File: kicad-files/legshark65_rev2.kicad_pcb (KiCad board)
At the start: 2 copper layers, 285.8 x 97 mm, 202 parts, among them J1 ARM JTAG, J2 Conn_01x04, SW1 K2-1187SQ-A4SW-06, SW2 PCM12SMTR, T2 53261-0471, U1 STM32F411CEU6, U2 MCP1700T-3302E/TT, U3 AT24C256C-SSHL-T, Y1 TAXM8M4RFDCET2T

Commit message: Started adding all of the components onto the board
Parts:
- removed J2: Conn_01x04, acheron_Connectors:PinHeader_1x4_P2.54mm_Vertical
- removed R2, R3: 0R, Resistor_SMD:R_0603_1608Metric
- J1: moved to F.Cu
- moved J1 177.1 mm to (278.6, 17.8), turned to 90 degrees
- moved T2 129.6 mm to (142.9, 38.1), turned to 0 degrees
- moved R15 106.6 mm to (172.3, 34.5)
- moved C3 105.4 mm to (152.1, 39.0)
- moved R9 105.4 mm to (153.5, 36.2)
- moved U2 105.4 mm to (157.4, 35.5)
- moved C5 105.4 mm to (152.1, 41.5)
- moved D1 105.4 mm to (156.9, 39.4)
- moved R4 105.4 mm to (153.5, 34.2)
- moved C17 101.6 mm to (168.7, 34.8)
- moved C16 100.5 mm to (130.0, 36.9), turned to 0 degrees
- moved SW2 100.3 mm to (172.0, 39.6)
- moved SW1 69.9 mm to (152.4, 76.2)
- moved R11 67.6 mm to (153.6, 71.4)
- moved C7 62.4 mm to (150.0, 71.4)
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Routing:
- net Net-(D_15-A): track 0.00 -> 24.5 mm
- net Net-(D_61-A): track 0.00 -> 24.4 mm
- net Net-(D_45-A): track 0.00 -> 23.8 mm
- net Net-(D_66-A): track 0.00 -> 20.1 mm
- net Net-(D_60-A): track 0.00 -> 19.7 mm
- net Net-(D_68-A): track 0.00 -> 18.7 mm
- net Net-(D_64-A): track 0.00 -> 18.7 mm
- net Net-(D_44-A): track 0.00 -> 18.5 mm
- net Net-(D_67-A): track 0.00 -> 14.9 mm
- net Net-(D_65-A): track 0.00 -> 14.9 mm
- net Net-(D_37-A): track 0.00 -> 14.9 mm
- net Net-(D_43-A): track 0.00 -> 14.2 mm
- net Net-(D_69-A): track 0.00 -> 14.0 mm
- net Net-(D_63-A): track 0.00 -> 14.0 mm
- net Net-(D_58-A): track 0.00 -> 9.20 mm
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
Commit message: Started running some test routes
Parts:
- moved J1 273.6 mm to (7.50, 54.7)
- moved U2 28.8 mm to (128.6, 35.5)
- moved R4 26.6 mm to (127.4, 39.3)
- moved T2 26.2 mm to (116.7, 38.1), turned to 90 degrees
- moved R9 23.9 mm to (129.8, 39.3)
- moved C5 19.8 mm to (132.4, 39.3)
- moved D1 16.4 mm to (140.5, 39.3)
- moved C3 16.3 mm to (135.7, 39.3)
- moved C6 12.2 mm to (165.5, 73.0)
- moved C16 10.7 mm to (140.5, 34.5)
- moved R7 9.73 mm to (165.5, 75.3)
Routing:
- net row3: track 0.00 -> 281.0 mm
- net row1: track 0.00 -> 281.0 mm
- net row2: track 0.00 -> 266.7 mm
- net row0: track 0.00 -> 266.7 mm
- net row4: track 0.00 -> 242.9 mm
- net unconnected-(U1-PB10-Pad21): track 0.00 -> 146.3 mm
- net BOOT1: track 0.00 -> 144.6 mm
- net unconnected-(U1-PB1-Pad19): track 0.00 -> 125.0 mm
- net unconnected-(U1-PA15-Pad38): track 0.00 -> 118.1 mm
- net unconnected-(U1-PB0-Pad18): track 0.00 -> 105.5 mm
- net unconnected-(U1-PB3-Pad39): track 0.00 -> 98.8 mm
- net unconnected-(U1-PA7-Pad17): track 0.00 -> 83.7 mm
- net unconnected-(U1-PB4-Pad40): track 0.00 -> 79.5 mm
- net unconnected-(U1-PA6-Pad16): track 0.00 -> 66.9 mm
- net unconnected-(U1-PB5-Pad41): track 0.00 -> 60.3 mm
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
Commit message: Added more routing and planning
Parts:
- moved C16 61.2 mm to (201.7, 35.2), turned to 180 degrees
- moved T2 59.5 mm to (176.2, 37.9), turned to -90 degrees
- moved R4 39.5 mm to (166.9, 40.2)
- moved R9 39.5 mm to (169.3, 40.2)
- moved C3 34.6 mm to (170.3, 38.2)
- moved C5 31.5 mm to (163.9, 39.2)
- moved U2 31.1 mm to (159.6, 38.6)
- moved D1 25.8 mm to (166.1, 36.6), turned to 0 degrees
- moved R15 19.1 mm to (172.8, 15.4)
- moved SW2 19.1 mm to (172.5, 20.5)
- moved C17 19.1 mm to (169.2, 15.7)
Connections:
- C1 pad 1: Net-(U1-PD1/OSC_OUT) -> GND
- C1 pad 2: GND -> Net-(U1-PD1/OSC_OUT)
- J1 pad 1: SWDIO -> SWCLK
- J1 pad 10: GND -> NRST
- J1 pad 2: SWCLK -> SWDIO
- J1 pad 5: BOOT0 -> BOOT1
- J1 pad 6: BOOT1 -> BOOT0
- J1 pad 9: NRST -> GND
- T2 pad 2: D+ -> D-
- T2 pad 3: D- -> D+
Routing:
- net D-: track 0.00 -> 41.7 mm
- net D+: track 0.00 -> 41.7 mm
- net unconnected-(U1-PB15/SPI2_MOSI-Pad28): track 0.00 -> 40.2 mm, vias 0 -> 2
- net unconnected-(U1-PB14-Pad27): track 0.00 -> 20.7 mm
- net unconnected-(U1-PC15/OSC32_OUT-Pad4): track 8.69 -> 28.4 mm, vias 0 -> 2
- net GND: track 3.02 -> 19.1 mm, vias 7 -> 10
- net SWCLK: track 0.00 -> 12.0 mm
- net SWDIO: track 0.00 -> 10.2 mm
- net 3V3: track 2.93 -> 6.25 mm, vias 0 -> 4
- net unconnected-(U1-PB12-Pad25): track 0.00 -> 3.11 mm
- net unconnected-(U1-PC14/OSC32_IN-Pad3): track 6.55 -> 8.98 mm
- net BOOT1: track 144.6 -> 142.7 mm
- net row2: track 266.7 -> 267.8 mm, vias 0 -> 2
- net unconnected-(U1-PB1-Pad19): track 125.0 -> 126.0 mm

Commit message: Started connecting more stuff
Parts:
- C1, C10, C11, C12, C13, C14, C15, C17, C2, C6, C7, C9: footprint Capacitor_SMD:C_0603_1608Metric_Pad1.08x0.95mm_HandSolder -> Capacitor_SMD:C_0402_1005Metric_Pad0.74x0.62mm_HandSolder
- C3, C5: footprint Capacitor_SMD:C_0603_1608Metric -> Capacitor_SMD:C_0402_1005Metric_Pad0.74x0.62mm_HandSolder
- R1, R11, R15, R5, R6, R7, R8: footprint Resistor_SMD:R_0603_1608Metric -> Resistor_SMD:R_0402_1005Metric_Pad0.72x0.64mm_HandSolder
- R4, R9: footprint Resistor_SMD:R_0402_1005Metric -> Resistor_SMD:R_0402_1005Metric_Pad0.72x0.64mm_HandSolder
- moved R6 117.0 mm to (21.8, 57.5)
- moved R5 101.5 mm to (158.9, 34.7), turned to -90 degrees
- moved R1 85.4 mm to (152.2, 46.6), turned to -90 degrees
- moved C10 80.9 mm to (157.7, 50.1), turned to -90 degrees
- moved C11 78.5 mm to (145.2, 52.7), turned to 0 degrees
- moved C15 77.3 mm to (145.1, 54.5), turned to 90 degrees
- moved C14 72.2 mm to (159.6, 61.3), turned to 0 degrees
- moved C9 69.2 mm to (159.6, 60.3)
- moved C12 65.6 mm to (148.2, 68.7)
- moved C13 58.6 mm to (145.8, 68.7), turned to 0 degrees
- moved R15 57.4 mm to (171.0, 72.8)
- moved C17 57.0 mm to (168.1, 72.7)
- moved SW2 55.7 mm to (171.4, 76.2)
- moved R8 22.0 mm to (199.4, 72.6)
- moved C6 20.3 mm to (185.7, 71.5)
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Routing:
- net 3V3: track 6.25 -> 64.4 mm, vias 4 -> 7
- net Net-(U1-PB6--I2C1_SCL): track 0.00 -> 26.9 mm, vias 0 -> 2
- net Net-(U1-PB7--I2C1_SDA): track 0.00 -> 25.8 mm, vias 0 -> 2
- net BOOT0: track 0.00 -> 24.9 mm, vias 0 -> 2
- net row2: track 267.8 -> 247.7 mm
- net GND: track 19.1 -> 30.5 mm
- net NRST: track 0.00 -> 10.2 mm
- net unconnected-(U1-PA1-Pad11): track 0.00 -> 9.26 mm
- net unconnected-(U1-PA0-WKUP-Pad10): track 0.00 -> 8.75 mm
- net unconnected-(U1-PA2-Pad12): track 0.00 -> 7.37 mm
- net Net-(U1-VCAP_1): track 0.00 -> 3.44 mm
- net Net-(U1-PD1/OSC_OUT): track 3.93 -> 5.41 mm
- net Net-(U1-PD0/OSC_IN): track 5.81 -> 7.29 mm

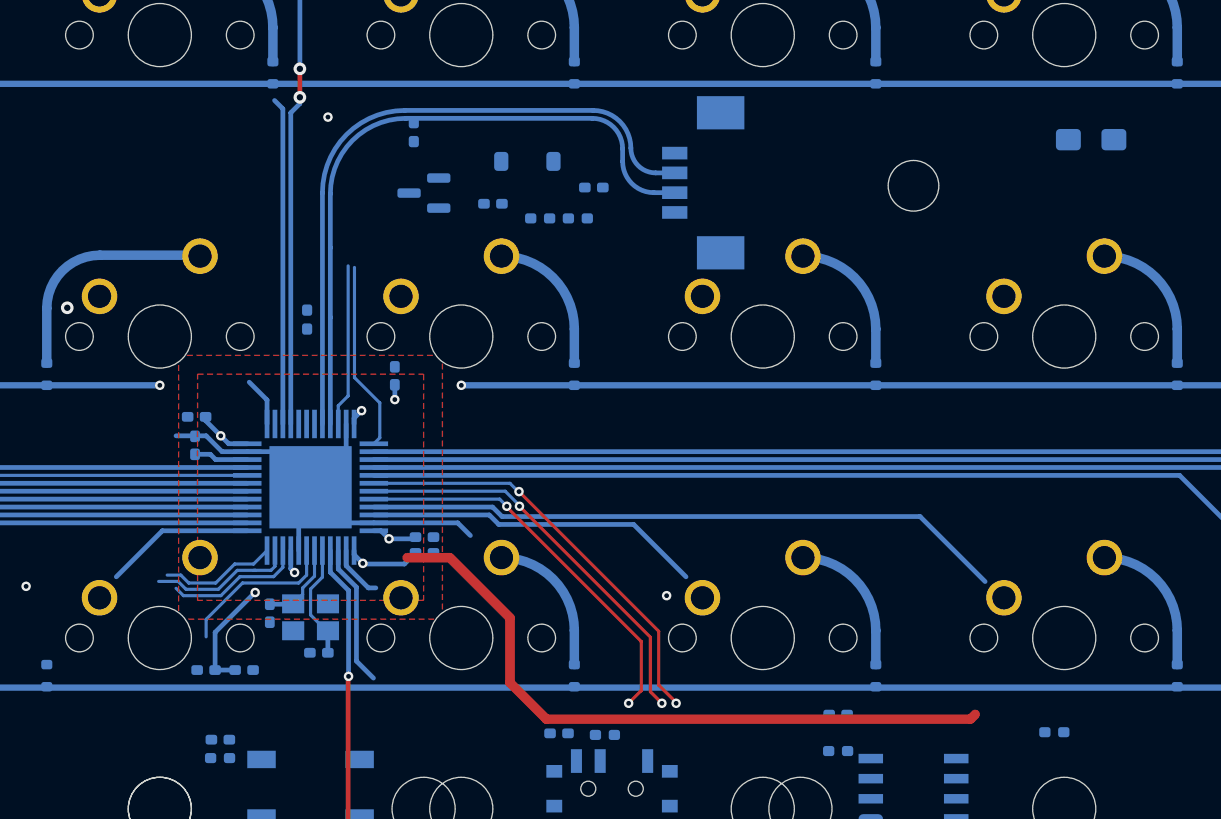
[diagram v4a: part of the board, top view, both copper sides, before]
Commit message: Started routing NRST BOOT0 BOOT1 etc
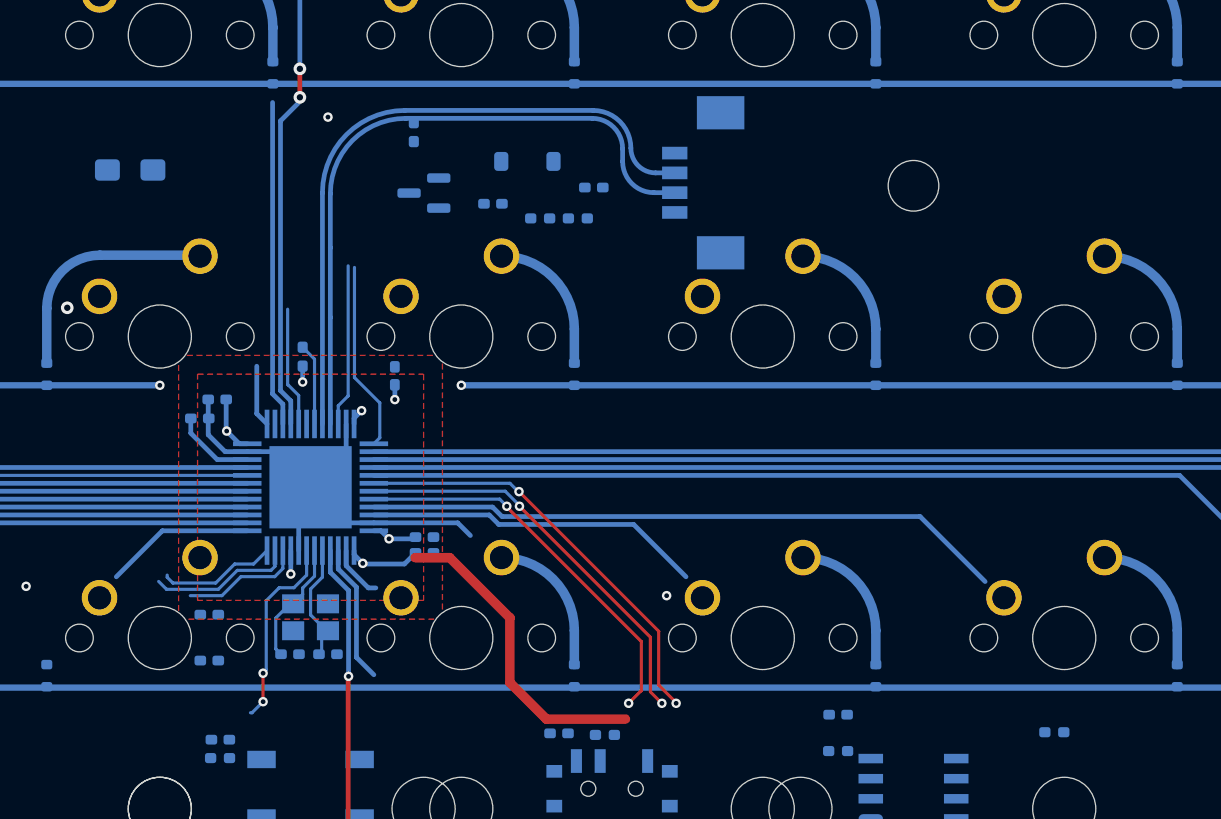
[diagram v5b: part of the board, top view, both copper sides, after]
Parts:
- moved C16 60.8 mm to (141.0, 37.1)
- moved C12 4.13 mm to (146.0, 65.2)
- moved C1 2.89 mm to (151.1, 67.7), turned to 180 degrees
- moved R1 2.36 mm to (151.9, 48.9), turned to 90 degrees
- moved C15 1.73 mm to (145.4, 52.8), turned to 0 degrees
- moved C11 1.70 mm to (146.5, 51.6)
- moved C13 0.63 mm to (146.0, 68.1)
- moved C2 0.58 mm to (153.5, 67.7), turned to 0 degrees
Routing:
- net 3V3: track 64.4 -> 35.6 mm
- net unconnected-(U1-PA8-Pad29): track 0.00 -> 7.54 mm
- net Net-(U1-PA10): track 0.00 -> 5.16 mm
- net Net-(U1-PD1/OSC_OUT): track 5.41 -> 7.82 mm
- net NRST: track 10.2 -> 12.3 mm, vias 0 -> 2
- net Net-(U1-VCAP_1): track 3.44 -> 5.19 mm
- net unconnected-(U1-PA0-WKUP-Pad10): track 8.75 -> 7.70 mm
- net unconnected-(U1-PB12-Pad25): track 3.11 -> 3.92 mm
- net unconnected-(U1-PB15/SPI2_MOSI-Pad28): track 40.2 -> 40.7 mm

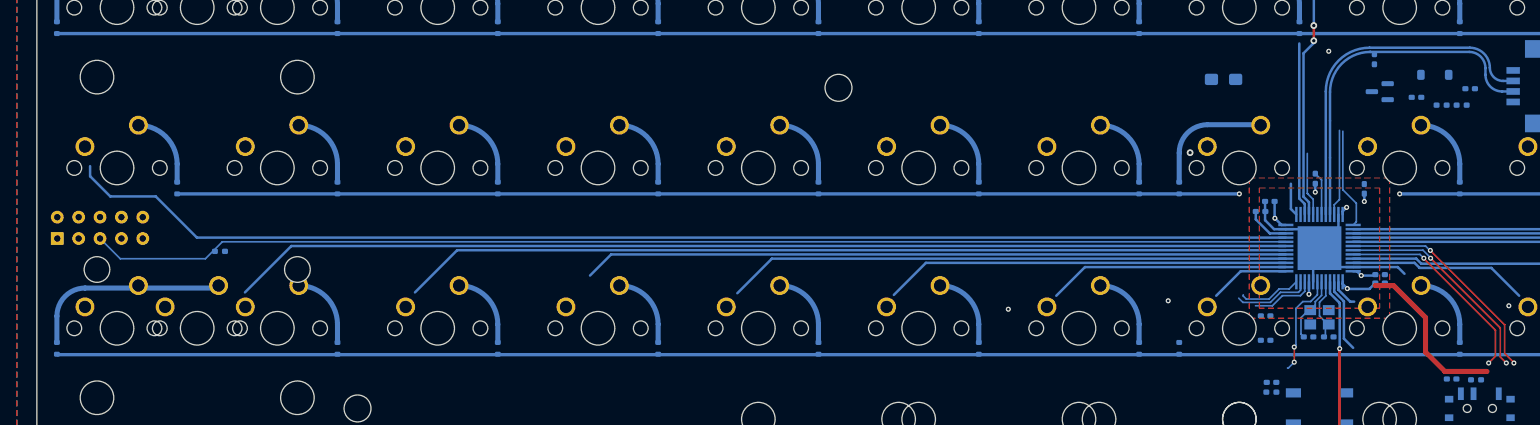
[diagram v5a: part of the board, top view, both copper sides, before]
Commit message: Moved the JTAG and routed NRST and BOOT0 to it
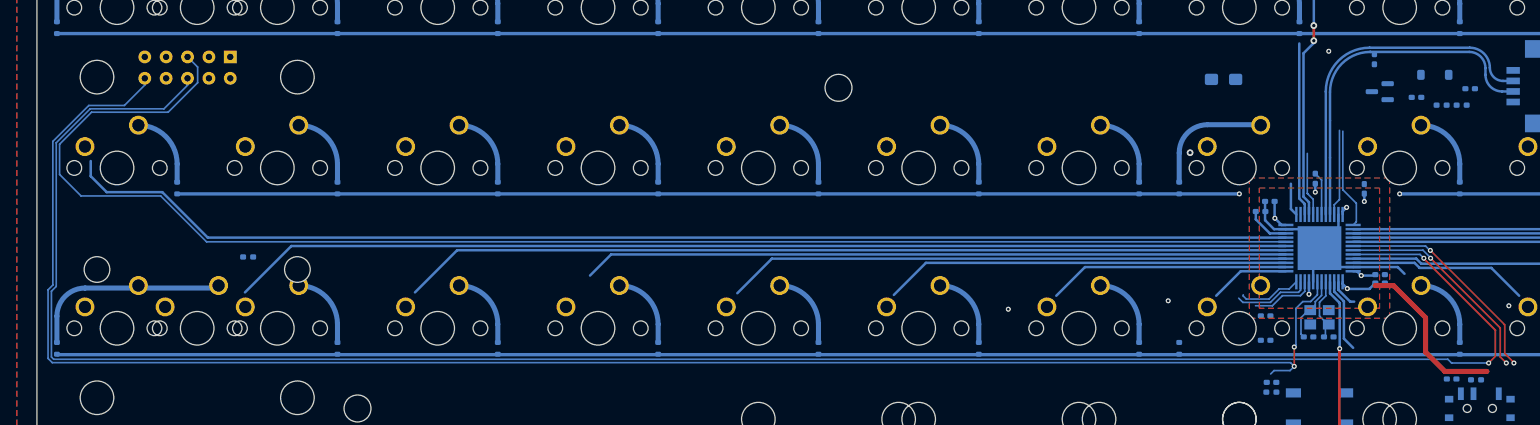
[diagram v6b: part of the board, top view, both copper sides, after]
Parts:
- moved J1 21.7 mm to (17.9, 35.7), turned to -90 degrees
- moved R6 3.41 mm to (25.1, 58.2)
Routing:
- net BOOT0: track 24.9 -> 240.9 mm
- net NRST: track 12.3 -> 203.9 mm
- net BOOT1: track 142.7 -> 175.6 mm
- net unconnected-(U1-PB10-Pad21): track 146.3 -> 146.8 mm

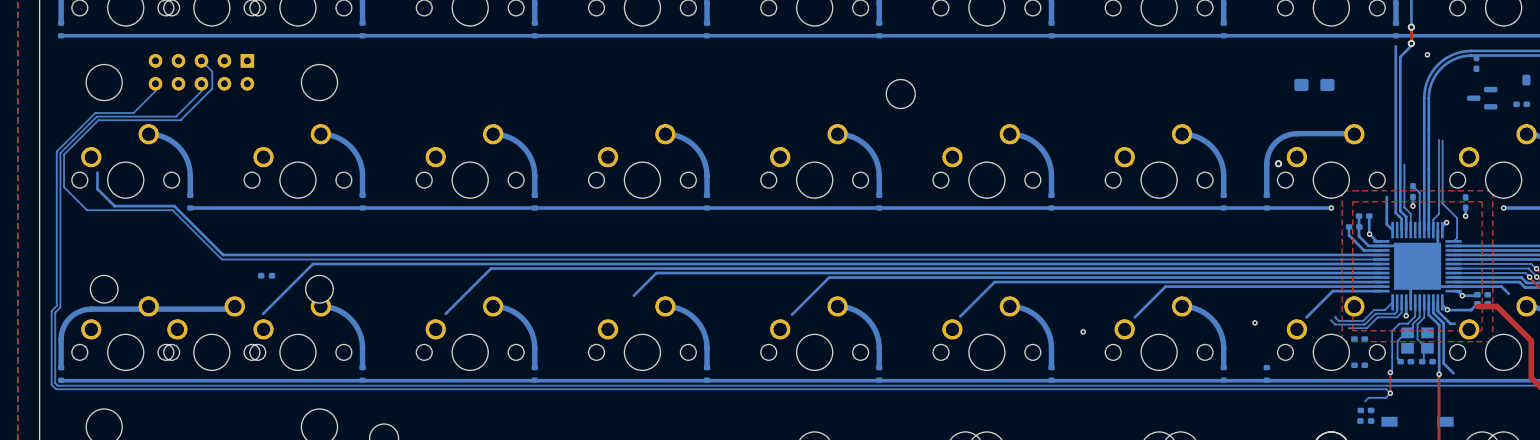
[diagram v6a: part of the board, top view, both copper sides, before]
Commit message: Route swdo swidioidaod
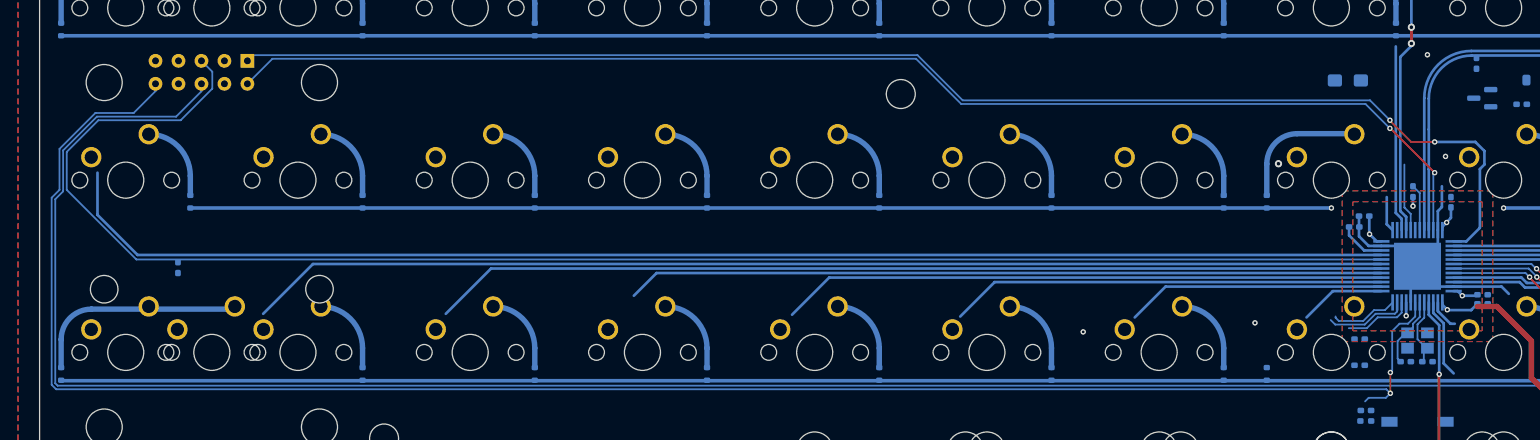
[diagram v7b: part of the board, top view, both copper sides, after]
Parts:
- moved R6 9.84 mm to (15.3, 57.3), turned to 90 degrees
- moved C16 3.73 mm to (144.7, 36.6)
- moved C10 1.63 mm to (156.1, 50.1)
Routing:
- net SWCLK: track 12.0 -> 153.7 mm, vias 0 -> 2
- net SWDIO: track 10.2 -> 144.1 mm, vias 0 -> 2
- net GND: track 30.7 -> 35.7 mm, vias 10 -> 11
- net unconnected-(U1-PB10-Pad21): track 146.8 -> 148.5 mm
- net 3V3: track 35.6 -> 36.5 mm, vias 7 -> 6
